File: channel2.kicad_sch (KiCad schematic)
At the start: 58 parts, among them IC3 TLV73325PDBVT, IC4 TLV73312PDBVT, J4 47151-1001, J5 5051101992, U4 TC358742XBG, U5 TPD8S009DSMR, U6 PCA9517ATP, Y2 7C-27.000MBB-T

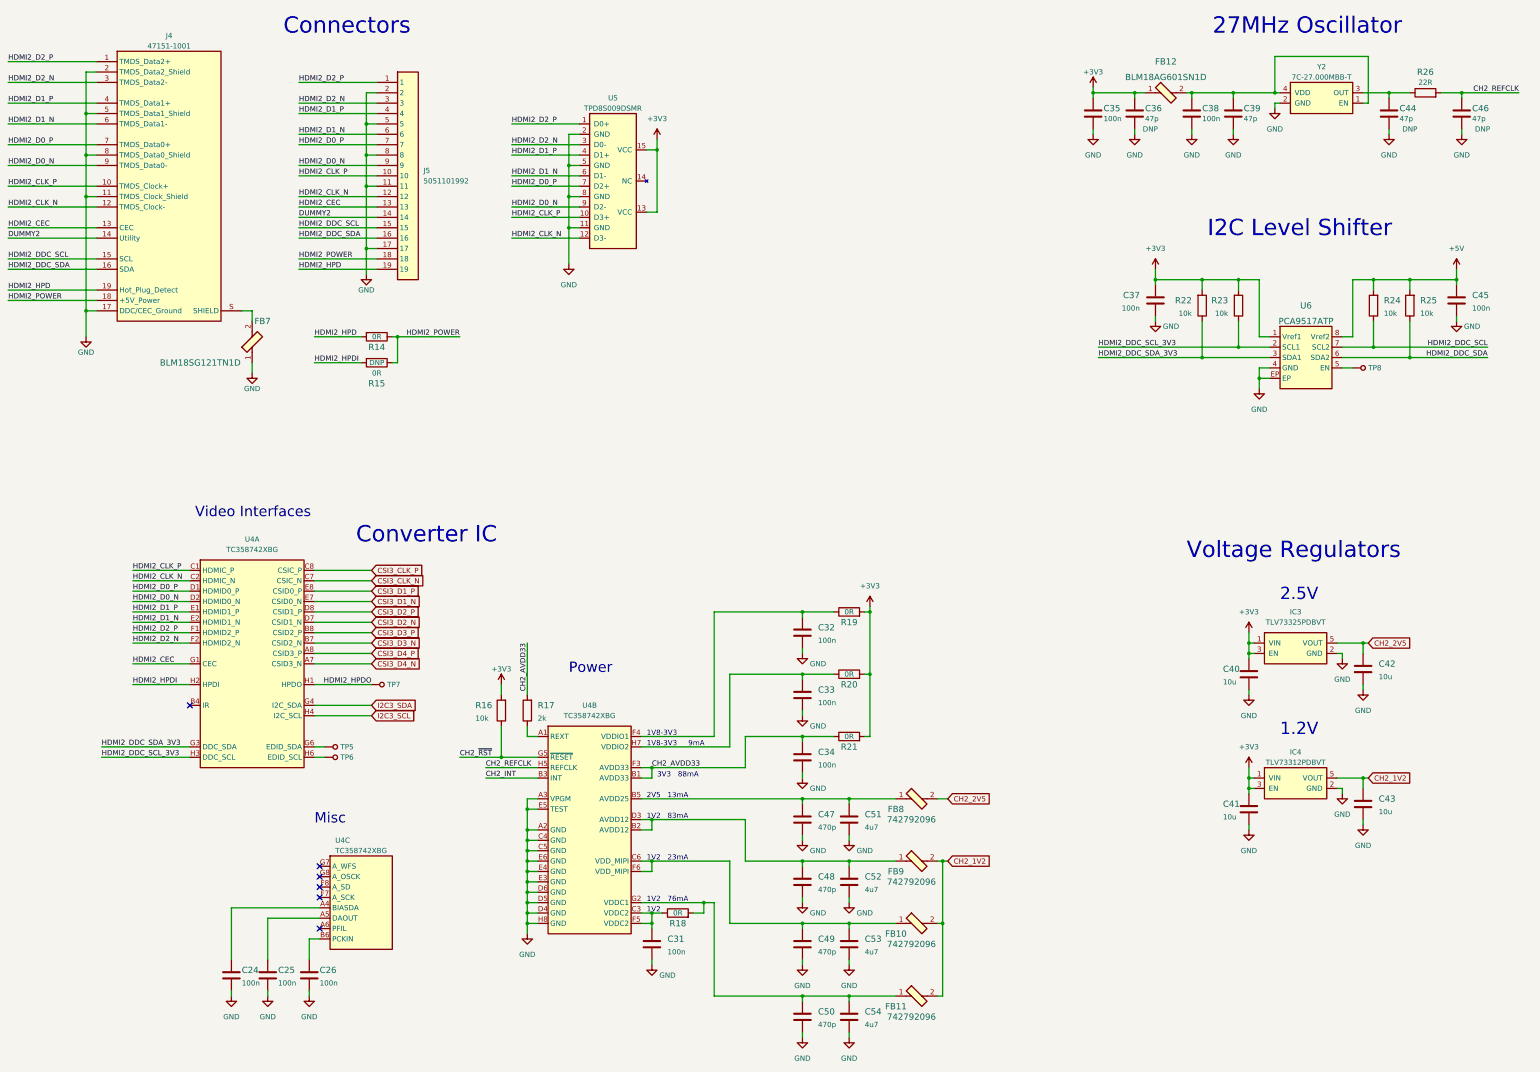
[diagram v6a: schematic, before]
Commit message: Introduce component standardization
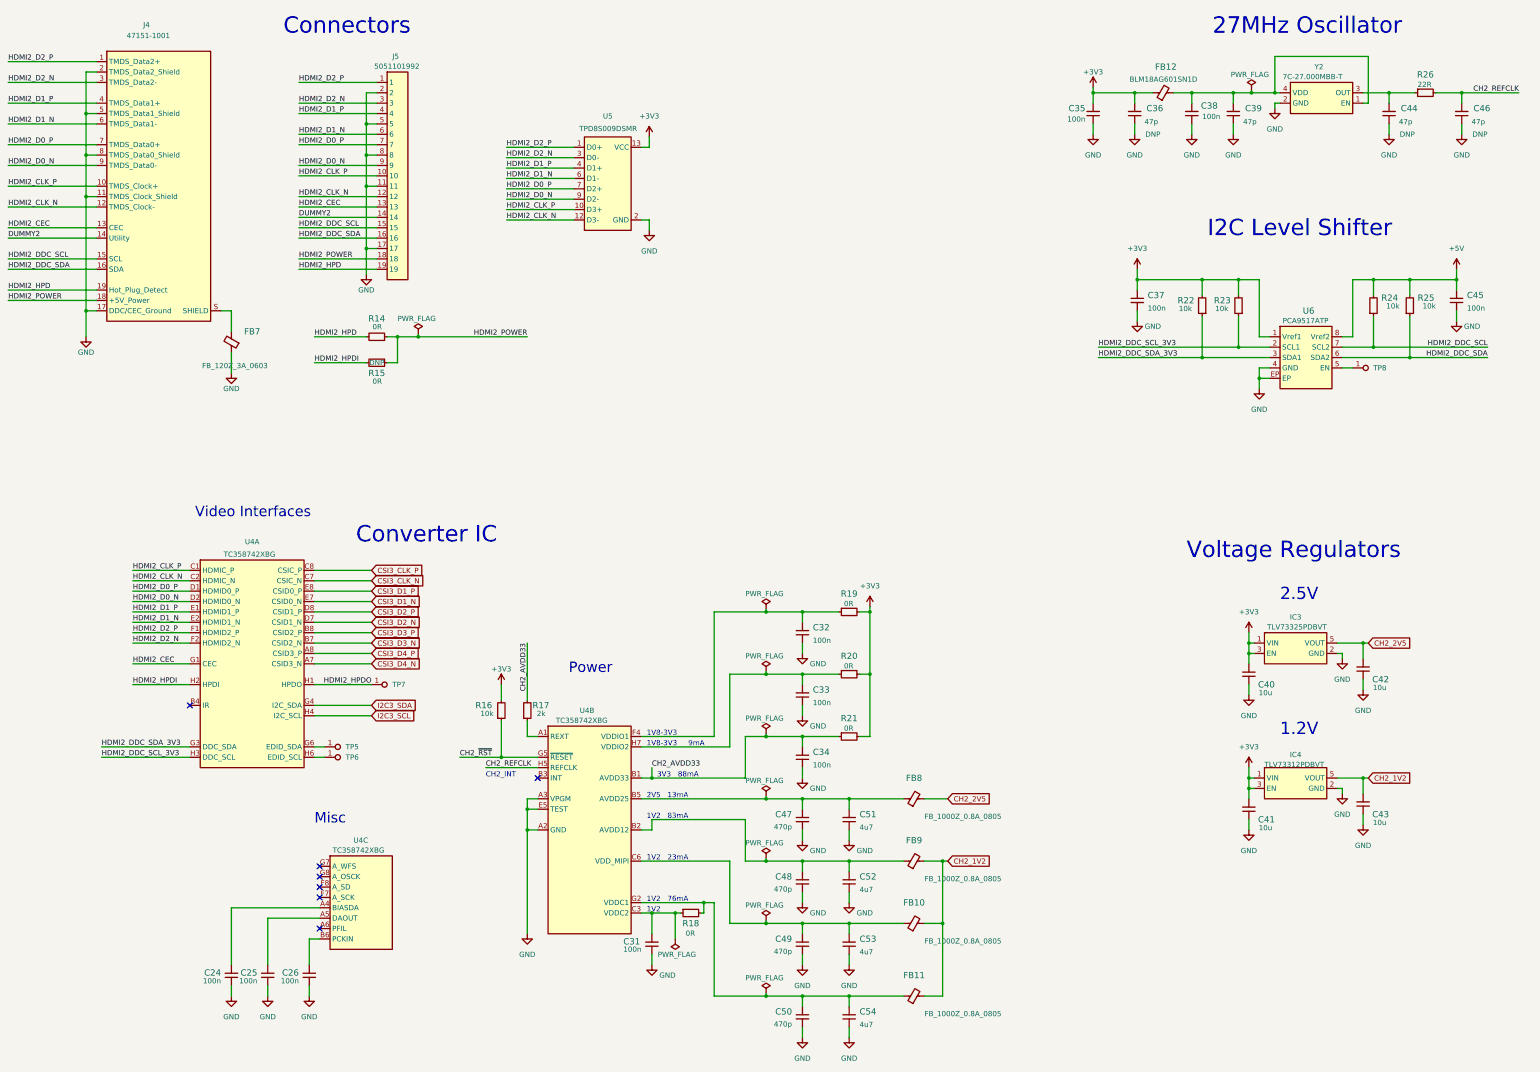
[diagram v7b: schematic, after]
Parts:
- C24, C25, C26, C31, C32, C33, C34, C35, C37, C38, C45: footprint antmicro-hdmi-mipi-bridge-hw-footprints:0402-cap -> antmicro-hdmi-mipi-bridge-hw-footprints:C_0402_1005Metric; Author (none) -> Antmicro; Dielectric (none) -> X5R; License (none) -> Apache-2.0; Voltage (none) -> 50V
- C36, C39, C44, C46: footprint antmicro-hdmi-mipi-bridge-hw-footprints:0402-cap -> antmicro-hdmi-mipi-bridge-hw-footprints:C_0402_1005Metric; Author (none) -> Antmicro; Dielectric (none) -> C0G; License (none) -> Apache-2.0; MPN C0402C470J5GACTU -> GRM1555C1E470JA01D; Manufacturer KEMET -> Murata
- C40, C41, C42, C43, C51, C52, C53, C54: footprint antmicro-hdmi-mipi-bridge-hw-footprints:0603-cap -> antmicro-hdmi-mipi-bridge-hw-footprints:C_0603_1608Metric; Author (none) -> Antmicro; License (none) -> Apache-2.0
- C47, C48, C49, C50: footprint antmicro-hdmi-mipi-bridge-hw-footprints:0402-cap -> antmicro-hdmi-mipi-bridge-hw-footprints:C_0402_1005Metric; Author (none) -> Antmicro; License (none) -> Apache-2.0; Manufacturer WALSIN -> Walsin
- FB10, FB11, FB8, FB9: value 742792096 -> FB_1000Z_0.8A_0805; footprint antmicro-hdmi-mipi-bridge-hw-footprints:0805-res -> antmicro-hdmi-mipi-bridge-hw-footprints:FB_0805_2012Metric; symbol antmicro-hdmi-mipi-bridge-hw:742792096 -> antmicro-hdmi-mipi-bridge-hw:FB_1000Z_0.8A_0805; Author (none) -> Antmicro; License (none) -> Apache-2.0; Manufacturer Wurth Electronic -> Würth Elektronik
- FB12: value BLM18AG601SN1D -> FB_600Z_0.5A_0603; footprint antmicro-hdmi-mipi-bridge-hw-footprints:0603 -> antmicro-hdmi-mipi-bridge-hw-footprints:FB_0603_1608Metric; symbol antmicro-hdmi-mipi-bridge-hw:BLM18AG601SN1D -> antmicro-hdmi-mipi-bridge-hw:FB_600Z_0.5A_0603; Author (none) -> Antmicro; License (none) -> Apache-2.0; Manufacturer Murata Electronics North America -> Murata
- FB7: value BLM18SG121TN1D -> FB_120Z_3A_0603; footprint antmicro-hdmi-mipi-bridge-hw-footprints:0603-res -> antmicro-hdmi-mipi-bridge-hw-footprints:FB_0603_1608Metric; symbol antmicro-hdmi-mipi-bridge-hw:BLM18SG121TN1D -> antmicro-hdmi-mipi-bridge-hw:FB_120Z_3A_0603; Author (none) -> Antmicro; License (none) -> Apache-2.0; Manufacturer Murata Electronics North America -> Murata
- IC3, IC4, J4, J5, U4, U5, Y2: Author (none) -> Antmicro; License (none) -> Apache-2.0
- R14, R15, R18, R19, R20, R21: footprint antmicro-hdmi-mipi-bridge-hw-footprints:0603-res -> antmicro-hdmi-mipi-bridge-hw-footprints:R_0603_1608Metric; Author (none) -> Antmicro; Current (none) -> 1A; License (none) -> Apache-2.0; Manufacturer BOURNS -> Bourns
- R16, R22, R23, R24, R25: footprint antmicro-hdmi-mipi-bridge-hw-footprints:0402-res -> antmicro-hdmi-mipi-bridge-hw-footprints:R_0402_1005Metric; Author (none) -> Antmicro; License (none) -> Apache-2.0; MPN CRCW040210K0FKEDHP -> CR0402-FX-1002GLF; Manufacturer VISHAY -> Bourns; Tolerance (none) -> 1%
- R17: footprint antmicro-hdmi-mipi-bridge-hw-footprints:0402-res -> antmicro-hdmi-mipi-bridge-hw-footprints:R_0402_1005Metric; Author (none) -> Antmicro; License (none) -> Apache-2.0; MPN CRCW04022K00FKED -> CR0402-FX-2001GLF; Manufacturer VISHAY -> Bourns; Tolerance (none) -> 1%
- R26: footprint antmicro-hdmi-mipi-bridge-hw-footprints:0402-res -> antmicro-hdmi-mipi-bridge-hw-footprints:R_0402_1005Metric; Author (none) -> Antmicro; License (none) -> Apache-2.0; MPN CRCW040222R0FKED -> CR0402-FX-22R0GLF; Manufacturer VISHAY -> Bourns; Tolerance (none) -> 1%
- TP5, TP6, TP7, TP8: value TP_SMD_0_75MM -> TP_0.75mm_SMD; footprint antmicro-hdmi-mipi-bridge-hw-footprints:Testpoint_smd_0_75mm -> antmicro-hdmi-mipi-bridge-hw-footprints:TP_SMD_0.75mm; symbol antmicro-hdmi-mipi-bridge-hw:TP_SMD_0_75MM -> antmicro-hdmi-mipi-bridge-hw:TP_0.75mm_SMD; Author (none) -> Antmicro; License (none) -> Apache-2.0
- U6: Author (none) -> Antmicro; License (none) -> Apache-2.0; Manufacturer NXP USA Inc. -> NXP
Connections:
- net +3V3: now also C35.2, C36.2, C40.2, C41.2; no longer C35.1, C36.1, C40.1, C41.1
- net +5V: now also C45.2; no longer C45.1
- net CH2_1V2: now also C43.2; no longer C43.1
- net CH2_2V5: now also C42.2; no longer C42.1
- net CH2_AVDD33: now also C34.2; no longer C34.1
- net CH2_REFCLK: now also C46.2; no longer C46.1
- net GND: now also C24.1, C25.1, C26.1, C31.1, C32.1, C33.1, C34.1, C35.1, C36.1, C38.1, C39.1, C40.1, C41.1, C42.1, C43.1, C44.1, C45.1, C46.1, C47.2, C48.2, C49.2, C50.2, C51.1, C52.1, C53.1, C54.1; no longer C24.2, C25.2, C26.2, C31.2, C32.2, C33.2, C34.2, C35.2, C36.2, C38.2, C39.2, C40.2, C41.2, C42.2, C43.2, C44.2, C45.2, C46.2, C47.1, C48.1, C49.1, C50.1, C51.2, C52.2, C53.2, C54.2
- net at FB12.2, Y2.1 (EN), Y2.4 (VDD): now also C38.2, C39.2; no longer C38.1, C39.1
- net at U4.A4 (BIASDA): now also C24.2; no longer C24.1
- net at R20.1, U4.H7 (VDDIO2): now also C33.2; no longer C33.1
- net at FB10.1, U4.C6 (VDD_MIPI), U4.F6 (VDD_MIPI): now also C49.1, C53.2; no longer C49.2, C53.1
- net at FB9.1, U4.B2 (AVDD12), U4.D3 (AVDD12): now also C48.1, C52.2; no longer C48.2, C52.1
- net at FB11.1, R18.2, U4.G2 (VDDC1): now also C50.1, C54.2; no longer C50.2, C54.1
- net at R19.1, U4.F4 (VDDIO1): now also C32.2; no longer C32.1
- net at R18.1, U4.C3 (VDDC2), U4.F5 (VDDC2): now also C31.2; no longer C31.1
- net at FB8.1, U4.B5 (AVDD25): now also C47.1, C51.2; no longer C47.2, C51.1
- net at R26.1, Y2.3 (OUT): now also C44.2; no longer C44.1
- net at U4.A5 (DAOUT): now also C25.2; no longer C25.1
- net at U4.B6 (PCKIN): now also C26.2; no longer C26.1
- net CH2_INT: no longer names the net of U4.B3 (INT)
- no-connect marks 6 -> 7
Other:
- note added: "CH2_INT"
- title: Antmicro HDMI MIPI Bridge -> HDMI-MIPI Bridge
- moved on the sheet: C24, C25, C26, C31, C32, C33, C34, C35, C36, C37, C38, C39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
